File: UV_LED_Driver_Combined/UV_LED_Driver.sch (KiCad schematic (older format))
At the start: 0 parts

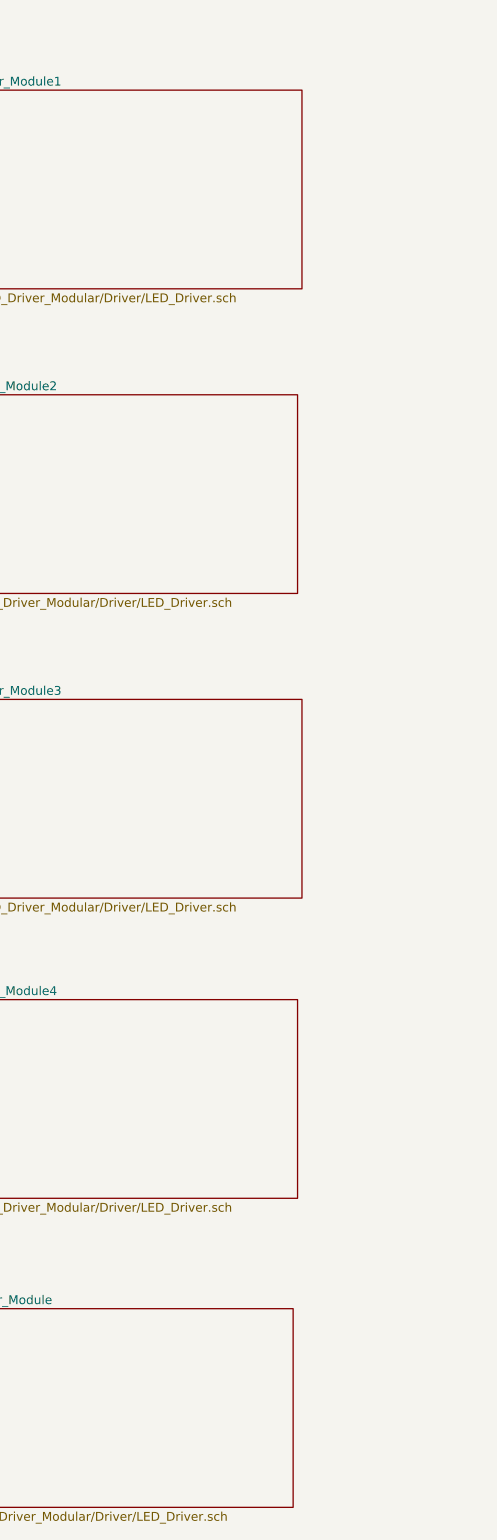
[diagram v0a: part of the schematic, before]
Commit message: Changed TO225 NPN (MJE340) to SOT223 NPN (PZT2222A)
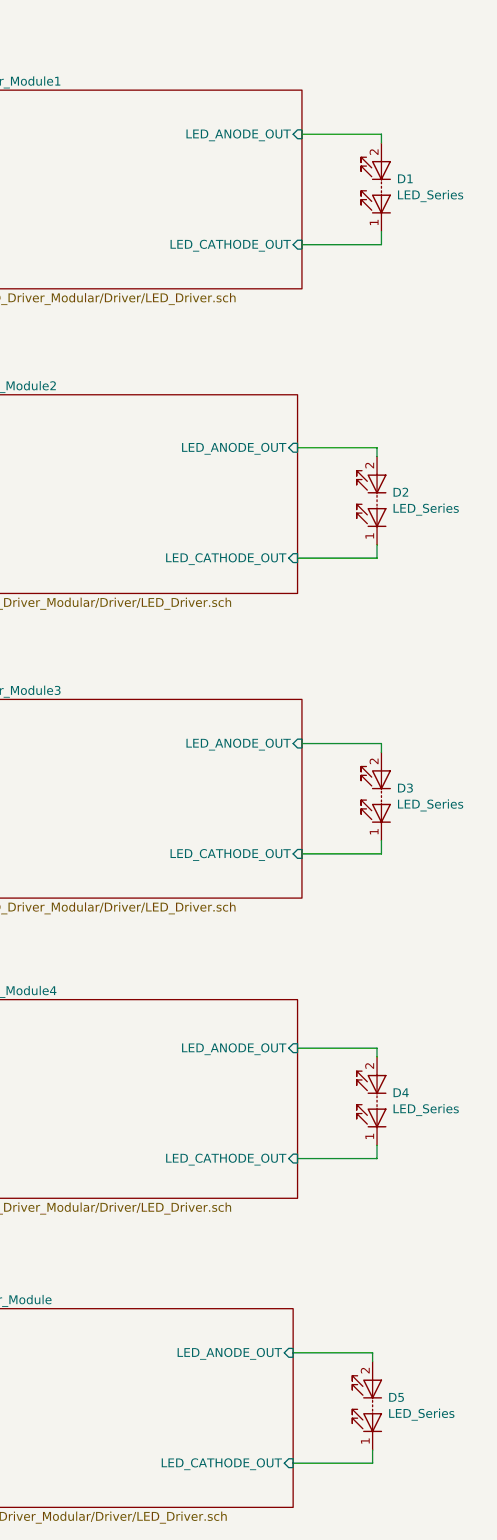
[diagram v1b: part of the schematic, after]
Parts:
- added D1, D2, D3, D4, D5: LED_Series, Connector_Molex:Molex_Mini-Fit_Jr_5569-02A2_2x01_P4.20mm_Horizontal, symbol Device:LED_Series
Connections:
- new net STD_LED_Driver_Module/LED_ANODE_OUT: D5.2 (A)
- new net STD_LED_Driver_Module/LED_CATHODE_OUT: D5.1 (K)
- new net UV_LED_Driver_Module1/LED_ANODE_OUT: D1.2 (A)
- new net UV_LED_Driver_Module1/LED_CATHODE_OUT: D1.1 (K)
- new net UV_LED_Driver_Module2/LED_ANODE_OUT: D2.2 (A)
- new net UV_LED_Driver_Module2/LED_CATHODE_OUT: D2.1 (K)
- new net UV_LED_Driver_Module3/LED_ANODE_OUT: D3.2 (A)
- new net UV_LED_Driver_Module3/LED_CATHODE_OUT: D3.1 (K)
- new net UV_LED_Driver_Module4/LED_ANODE_OUT: D4.2 (A)
- new net UV_LED_Driver_Module4/LED_CATHODE_OUT: D4.1 (K)
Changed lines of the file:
@@
 F2 "LED_CTRL" I L 7525 6250 50
 F3 "+5V" I L 7525 5775 50
+F4 "LED_ANODE_OUT" I R 9725 5750 50
+F5 "LED_CATHODE_OUT" I R 9725 6375 50
 $EndSheet
 $Sheet
@@
 F2 "LED_CTRL" I L 7550 7950 50
 F3 "+5V" I L 7550 7575 50
+F4 "LED_ANODE_OUT" I R 9750 7425 50
+F5 "LED_CATHODE_OUT" I R 9750 8050 50
 $EndSheet
 $Sheet
@@
 F2 "LED_CTRL" I L 7525 9650 50
 F3 "+5V" I L 7525 9300 50
+F4 "LED_ANODE_OUT" I R 9725 9150 50
+F5 "LED_CATHODE_OUT" I R 9725 9775 50
 $EndSheet
 Wire Wire Line
@@
 F2 "LED_CTRL" I L 7500 11400 50
 F3 "+5V" I L 7500 11050 50
+F4 "LED_ANODE_OUT" I R 9700 10875 50
+F5 "LED_CATHODE_OUT" I R 9700 11500 50
 $EndSheet
 Wire Wire Line
@@
 F2 "LED_CTRL" I L 7550 4450 50
 F3 "+5V" I L 7550 4075 50
+F4 "LED_ANODE_OUT" I R 9750 3975 50
+F5 "LED_CATHODE_OUT" I R 9750 4600 50
 $EndSheet
 $Comp
@@
 Wire Wire Line
 	3875 6225 3875 6700
+$Comp
+L Device:LED_Series D1
+U 1 1 5EA50B77
+P 10200 4275
+F 0 "D1" V 10246 4188 50  0000 R CNN
+F 1 "LED_Series" V 10155 4188 50  0000 R CNN
+F 2 "Connector_Molex:Molex_Mini-Fit_Jr_5569-02A2_2x01_P4.20mm_Horizontal" H 10100 4275 50  0001 C CNN
+F 3 "~" H 10100 4275 50  0001 C CNN
+	1    10200 4275
+	0    -1   -1   0
+$EndComp
+Wire Wire Line
+	9750 3975 10200 3975
+Wire Wire Line
+	10200 3975 10200 4025
+Wire Wire Line
+	9750 4600 10200 4600
+Wire Wire Line
+	10200 4600 10200 4525
+Wire Wire Line
+	9725 5750 10175 5750
+Wire Wire Line
+	10175 5750 10175 5800
+Wire Wire Line
+	9725 6375 10175 6375
+Wire Wire Line
+	10175 6375 10175 6300
+Wire Wire Line
+	9725 9150 10175 9150
+Wire Wire Line
+	10175 9150 10175 9200
+Wire Wire Line
+	9725 9775 10175 9775
+Wire Wire Line
+	10175 9775 10175 9700
+Wire Wire Line
+	9700 10875 10150 10875
+Wire Wire Line
+	10150 10875 10150 10925
+Wire Wire Line
+	9700 11500 10150 11500
+Wire Wire Line
+	10150 11500 10150 11425
+Wire Wire Line
+	9750 7425 10200 7425
+Wire Wire Line
+	10200 7425 10200 7475
+Wire Wire Line
+	9750 8050 10200 8050
+Wire Wire Line
+	10200 8050 10200 7975
+$Comp
+L Device:LED_Series D2
+U 1 1 5EA590C8
+P 10175 6050
+F 0 "D2" V 10221 5963 50  0000 R CNN
+F 1 "LED_Series" V 10130 5963 50  0000 R CNN
+F 2 "Connector_Molex:Molex_Mini-Fit_Jr_5569-02A2_2x01_P4.20mm_Horizontal" H 10075 6050 50  0001 C CNN
+F 3 "~" H 10075 6050 50  0001 C CNN
+	1    10175 6050
+	0    -1   -1   0
+$EndComp
+$Comp
+L Device:LED_Series D3
+U 1 1 5EA59ECF
+P 10200 7725
+F 0 "D3" V 10246 7638 50  0000 R CNN
+F 1 "LED_Series" V 10155 7638 50  0000 R CNN
+F 2 "Connector_Molex:Molex_Mini-Fit_Jr_5569-02A2_2x01_P4.20mm_Horizontal" H 10100 7725 50  0001 C CNN
+F 3 "~" H 10100 7725 50  0001 C CNN
+	1    10200 7725
+	0    -1   -1   0
+$EndComp
+$Comp
+L Device:LED_Series D4
+U 1 1 5EA5A5FB
+P 10175 9450
+F 0 "D4" V 10221 9363 50  0000 R CNN
+F 1 "LED_Series" V 10130 9363 50  0000 R CNN
+F 2 "Connector_Molex:Molex_Mini-Fit_Jr_5569-02A2_2x01_P4.20mm_Horizontal" H 10075 9450 50  0001 C CNN
+F 3 "~" H 10075 9450 50  0001 C CNN
+	1    10175 9450
+	0    -1   -1   0
+$EndComp
+$Comp
+L Device:LED_Series D5
+U 1 1 5EA5AF86
+P 10150 11175
+F 0 "D5" V 10196 11088 50  0000 R CNN
+F 1 "LED_Series" V 10105 11088 50  0000 R CNN
+F 2 "Connector_Molex:Molex_Mini-Fit_Jr_5569-02A2_2x01_P4.20mm_Horizontal" H 10050 11175 50  0001 C CNN
+F 3 "~" H 10050 11175 50  0001 C CNN
+	1    10150 11175
+	0    -1   -1   0
+$EndComp
 $EndSCHEMATC
